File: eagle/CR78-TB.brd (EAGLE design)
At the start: 100.8 x 80.8 mm, 39 parts, among them Q1 2N3904, Q2 2N3904, Q4 2N3904, Q6 2N3904, Q7 2N3904

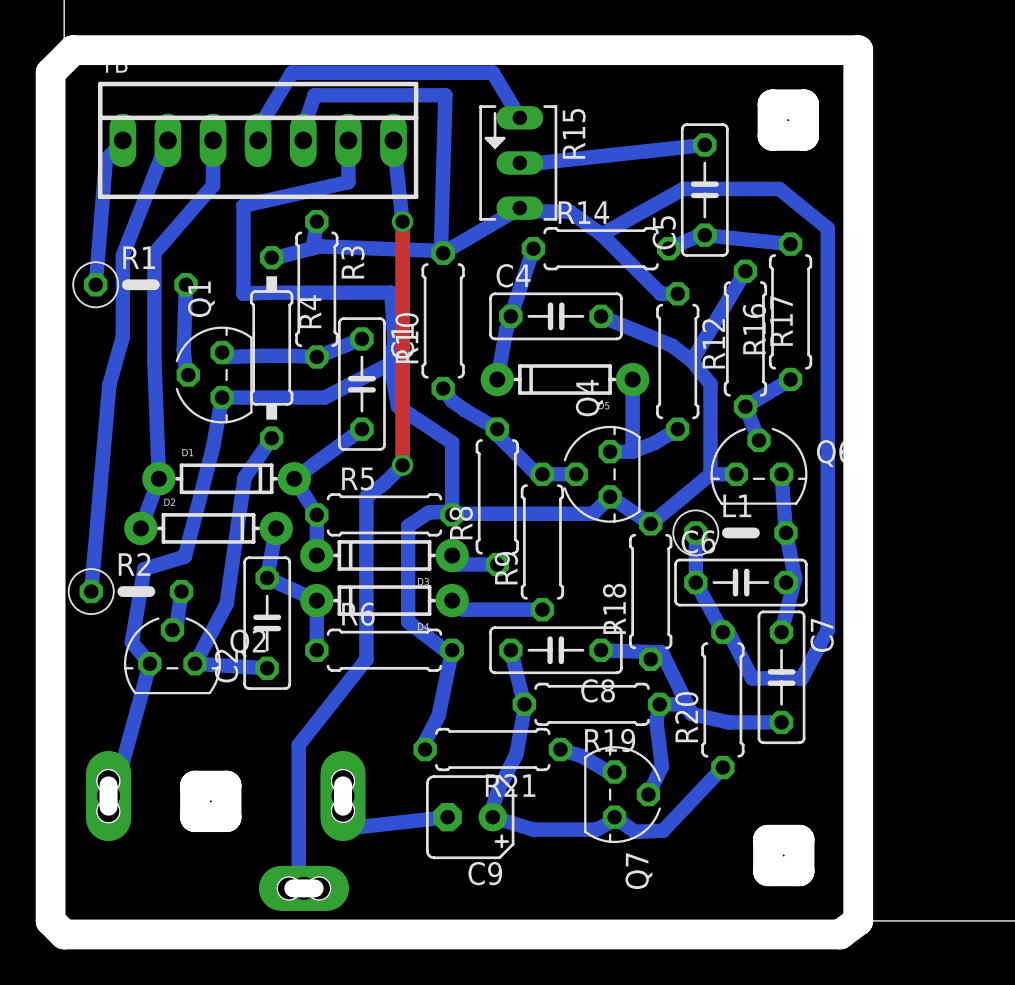
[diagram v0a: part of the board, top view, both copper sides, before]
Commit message: rewrote power and ground
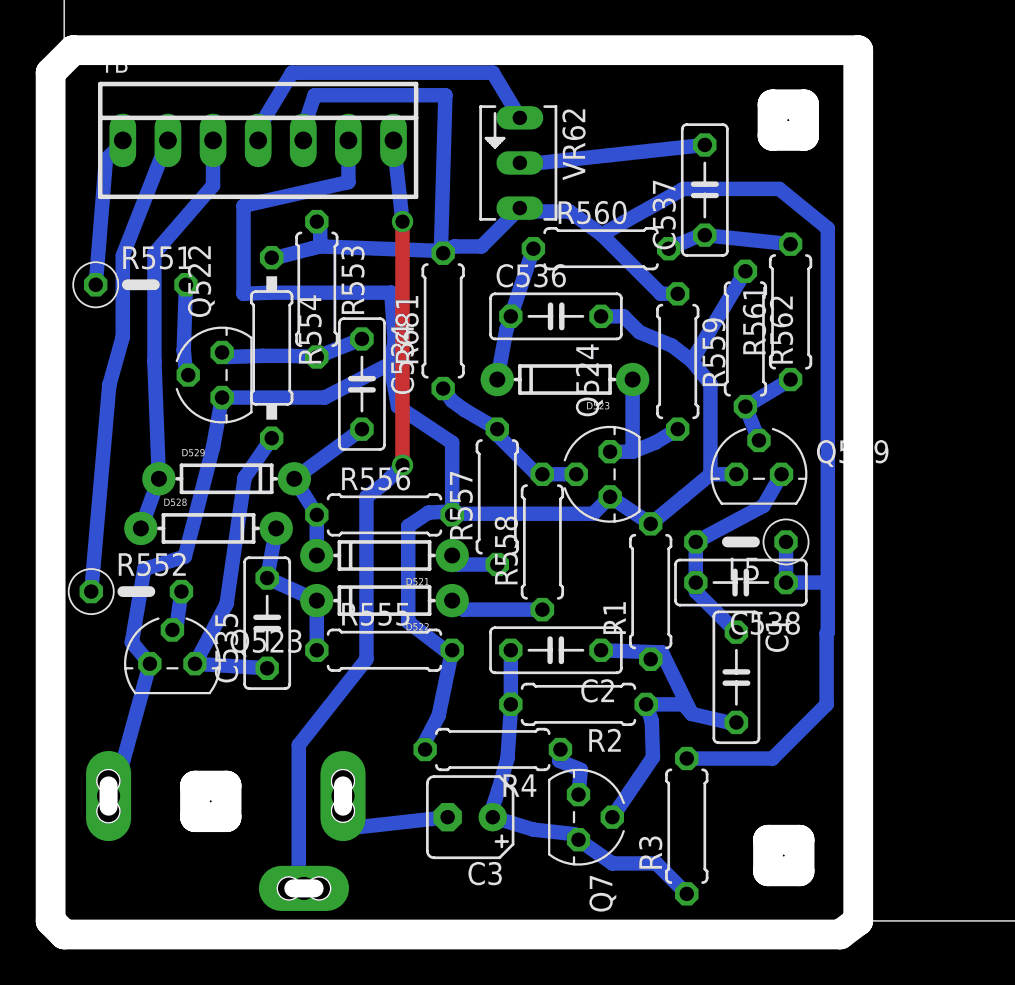
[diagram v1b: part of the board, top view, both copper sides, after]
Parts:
- removed C7: 473, rcl:C050-025X075
- removed C8: 47p, rcl:C050-025X075
- removed L1: 1R (40mH), rcl:0207/5V
- removed R18: 100k, rcl:0207/7
- removed R19: 470k, rcl:0207/7
- removed R20: 47k, rcl:0207/7
- removed R21: 220R, rcl:0207/7
- added C534, C535: 27n, rcl:C050-025X075
- added L5: 1R (40mH), rcl:0207/5V
- added R551, R552: 56k, rcl:0207/5V
- added R553: 10k, rcl:0207/7
- added R554: 10k, rcl:0207/10
- C1: value 27n -> 473
- C2: value 27n -> 47p
- R1: value 56k -> 100k; device rcl:0207/5V -> rcl:0207/7
- R2: value 56k -> 470k; device rcl:0207/5V -> rcl:0207/7
- R3: value 10k -> 47k
- R4: value 10k -> 220R; device rcl:0207/10 -> rcl:0207/7
- moved R3 36.7 mm to (35.1, 5.33), turned to 90 degrees
- moved R1 33.5 mm to (33.0, 18.5), turned to 90 degrees
- moved C1 26.8 mm to (37.8, 13.7)
- moved R4 25.8 mm to (24.1, 9.65), turned to 180 degrees
- moved R2 25.7 mm to (29.0, 12.2), turned to 180 degrees
- moved C2 16.3 mm to (27.7, 15.2), turned to 180 degrees
- moved Q7 2.40 mm to (29.0, 5.84)
- turned C538 to 180 degrees
- renumbered C4 to C536, C5 to C537, C6 to C538, C9 to C3, D1 to D529, D2 to D528, D3 to D521, D4 to D522, D5 to D523, Q1 to Q522, Q2 to Q523, Q4 to Q524, Q6 to Q509, R10 to R681, R12 to R559, R14 to R560, R15 to VR62, R16 to R561, R17 to R562, R5 to R556, R6 to R555, R8 to R557, R9 to R558
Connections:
- net +12V: now also L5.1, R3.2, R553.1, R554.1; no longer L1.1, R20.2, R3.1, R4.1
- net GND: now also R1.2, R4.2; no longer R18.2, R21.2
- net N$1: now also C535.2; no longer C2.2
- net N$11: now also R552.1; no longer R2.1
- net N$15: now also R4.1; no longer R21.1
- net N$16: now also C2.2, R2.2, R3.1; no longer C8.2, R19.2, R20.1
- net N$18: now also C1.2, C2.1, R1.1, R2.1; no longer C7.2, C8.1, R18.1, R19.1
- net N$20: now also C534.1, R553.2; no longer C1.1, R3.2
- net N$21: now also R551.2; no longer R1.2
- net N$22: now also C534.2; no longer C1.2
- net N$24: now also R551.1; no longer R1.1
- net N$46: now also C535.1, R554.2; no longer C2.1, R4.2
- net N$47: now also R552.2; no longer R2.2
- net N$6: now also C1.1, L5.2; no longer C7.1, L1.2
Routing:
- net N$16: track 25.0 -> 22.1 mm
- net +12V: track 97.7 -> 100.6 mm
- net N$6: track 9.61 -> 12.4 mm

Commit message: killed loose ends
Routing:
- net N$18: track 20.5 -> 18.5 mm
- net N$15: track 3.35 -> 2.85 mm
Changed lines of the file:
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@@
 <contactref element="Q7" pad="3"/>
 <contactref element="R4" pad="1"/>
-<wire x1="29.083" y1="8.509" x2="27.8765" y2="9.017" width="0.8128" layer="16"/>
-<wire x1="28.956" y1="7.112" x2="29.083" y2="8.509" width="0.8128" layer="16"/>
+<wire x1="28.321" y1="8.509" x2="27.8765" y2="9.017" width="0.8128" layer="16"/>
+<wire x1="28.956" y1="7.112" x2="28.321" y2="8.509" width="0.8128" layer="16"/>
 <wire x1="27.8765" y1="9.017" x2="27.94" y2="9.652" width="0.8128" layer="16"/>
 </signal>
@@
 <wire x1="24.0665" y1="6.223" x2="24.4475" y2="7.366" width="0.8128" layer="16"/>
 <wire x1="24.0665" y1="6.223" x2="24.13" y2="5.842" width="0.8128" layer="16"/>
-<wire x1="30.861" y1="3.2385" x2="33.3375" y2="3.2385" width="0.8128" layer="16"/>
-<wire x1="33.3375" y1="3.2385" x2="35.052" y2="1.524" width="0.8128" layer="16"/>
+<wire x1="30.861" y1="3.2385" x2="34.8615" y2="1.4605" width="0.8128" layer="16"/>
+<wire x1="34.8615" y1="1.4605" x2="35.052" y2="1.524" width="0.8128" layer="16"/>
 </signal>
 <signal name="N$18">
@@
 <wire x1="33.147" y1="9.2075" x2="30.861" y2="5.842" width="0.8128" layer="16"/>
 <wire x1="37.4015" y1="11.176" x2="37.846" y2="11.176" width="0.8128" layer="16"/>
-<wire x1="34.8615" y1="12.192" x2="35.33775" y2="11.65225" width="0.8128" layer="16"/>
-<wire x1="35.33775" y1="11.65225" x2="37.4015" y2="11.176" width="0.8128" layer="16"/>
-<wire x1="34.8615" y1="12.192" x2="32.766" y2="12.192" width="0.8128" layer="16"/>
-<wire x1="35.33775" y1="11.65225" x2="33.655" y2="15.113" width="0.8128" layer="16"/>
-<wire x1="33.655" y1="15.113" x2="30.226" y2="15.24" width="0.8128" layer="16"/>
-<wire x1="33.655" y1="15.113" x2="33.02" y2="14.732" width="0.8128" layer="16"/>
+<wire x1="32.8295" y1="12.446" x2="33.30575" y2="11.90625" width="0.8128" layer="16"/>
+<wire x1="33.30575" y1="11.90625" x2="37.4015" y2="11.176" width="0.8128" layer="16"/>
+<wire x1="32.8295" y1="12.446" x2="32.766" y2="12.192" width="0.8128" layer="16"/>
+<wire x1="33.30575" y1="11.90625" x2="32.893" y2="14.859" width="0.8128" layer="16"/>
+<wire x1="32.893" y1="14.859" x2="30.226" y2="15.24" width="0.8128" layer="16"/>
+<wire x1="32.893" y1="14.859" x2="33.02" y2="14.732" width="0.8128" layer="16"/>
 </signal>
 <signal name="N$19">
